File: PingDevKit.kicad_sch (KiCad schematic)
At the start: 47 parts, among them J101 POWER, J102 DEBUG, J103 PORT1, J104 FPGA, J105 ETHERNET, J106 SYNC, J107 SONAR+, J108 SONAR+, J109 SONAR-, J110 SONAR-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

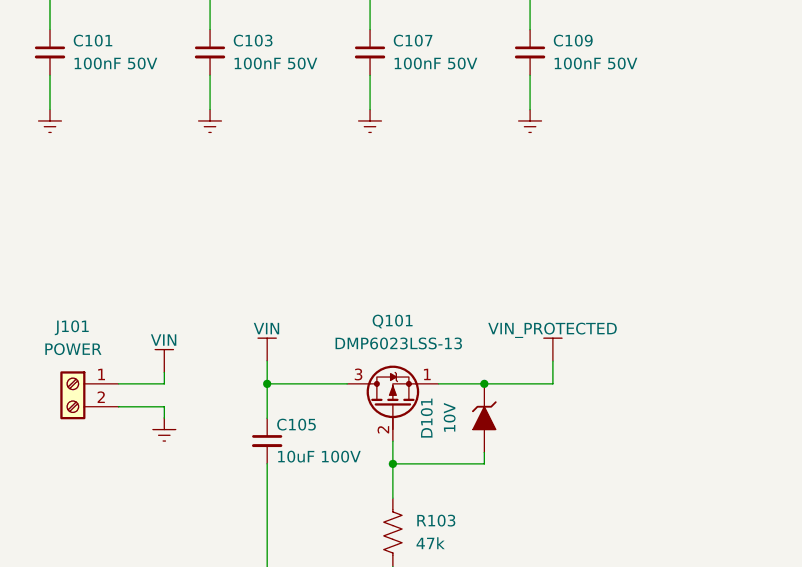
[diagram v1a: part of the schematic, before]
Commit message: ethernet MDI routing
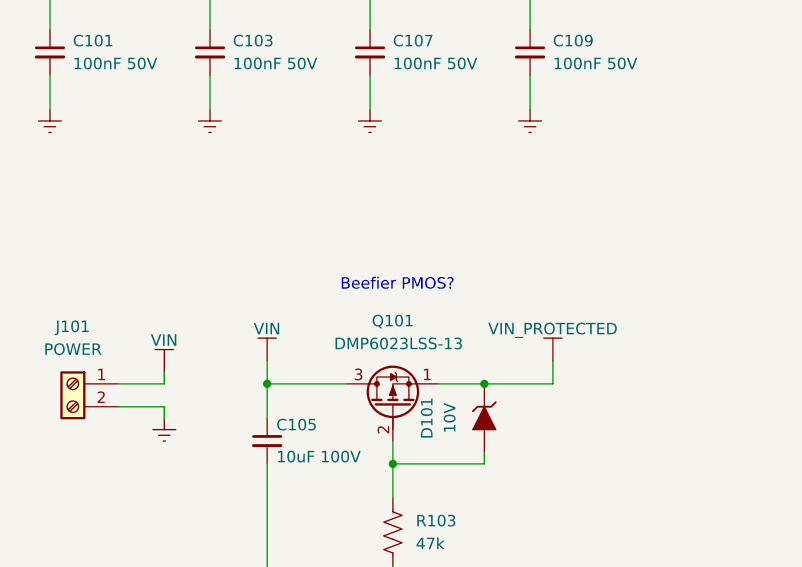
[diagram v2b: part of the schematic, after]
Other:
- note added: "Beefier PMOS?"
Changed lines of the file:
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@@
 		)
 	)
+	(text "Beefier PMOS?"
+		(exclude_from_sim no)
+		(at 69.088 57.658 0)
+		(effects
+			(font
+				(size 1.27 1.27)
+			)
+		)
+	)
 	(text "Gain is from 0 to 60dB from 0.1 to 0.85V "
 		(exclude_from_sim no)
@@
 			(justify right bottom)
 		)
+		(property "Netclass" "MDI"
+			(at 84.074 241.554 0)
+			(effects
+				(font
+					(size 1.27 1.27)
+					(italic yes)
+				)
+				(justify right)
+				(hide yes)
+			)
+		)
 	)
 	(label "ETH{100BASE-T}"
@@
 			(justify right bottom)
 		)
+		(property "Netclass" "MDI"
+			(at 84.074 251.714 0)
+			(effects
+				(font
+					(size 1.27 1.27)
+					(italic yes)
+				)
+				(justify right)
+				(hide yes)
+			)
+		)
 	)
 	(label "SWCLK"
@@
 			(justify right bottom)
 		)
+		(property "Netclass" "MDI"
+			(at 84.074 254.254 0)
+			(effects
+				(font
+					(size 1.27 1.27)
+					(italic yes)
+				)
+				(justify right)
+				(hide yes)
+			)
+		)
 	)
 	(label "OCTOSPI1{OCTOSPI}"
@@
 			(justify right bottom)
 		)
+		(property "Netclass" "MDI"
+			(at 84.074 249.174 0)
+			(effects
+				(font
+					(size 1.27 1.27)
+					(italic yes)
+				)
+				(justify right)
+				(hide yes)
+			)
+		)
 	)

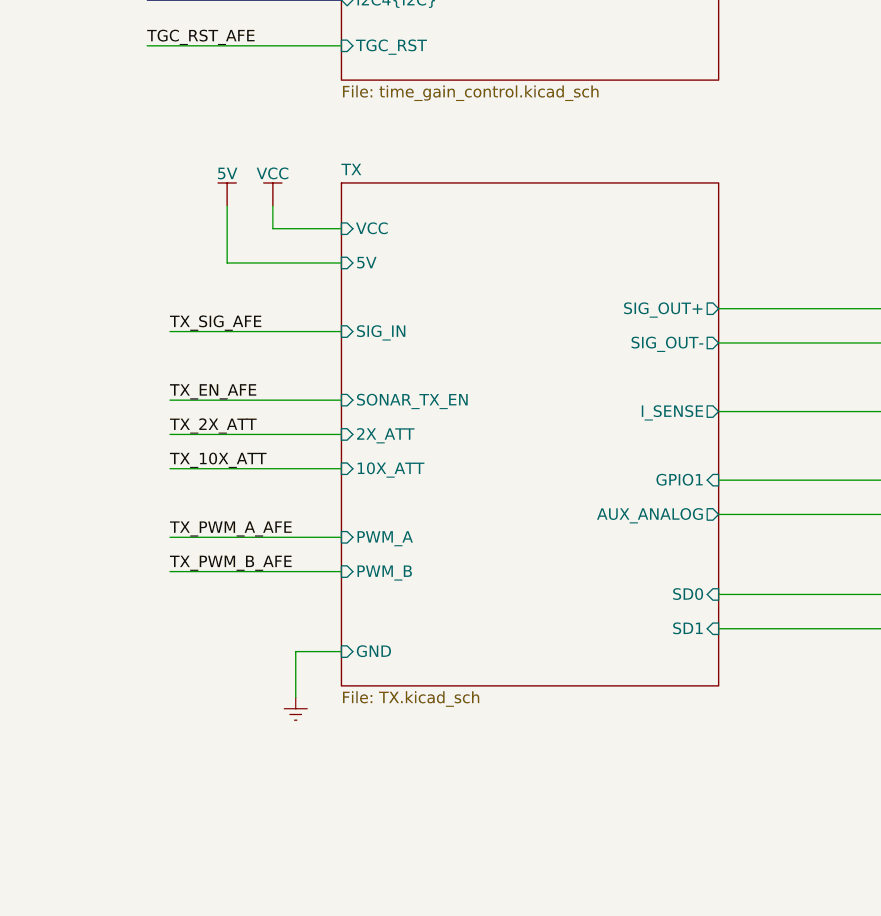
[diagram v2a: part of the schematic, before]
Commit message: bigger board outline + initial integration placements
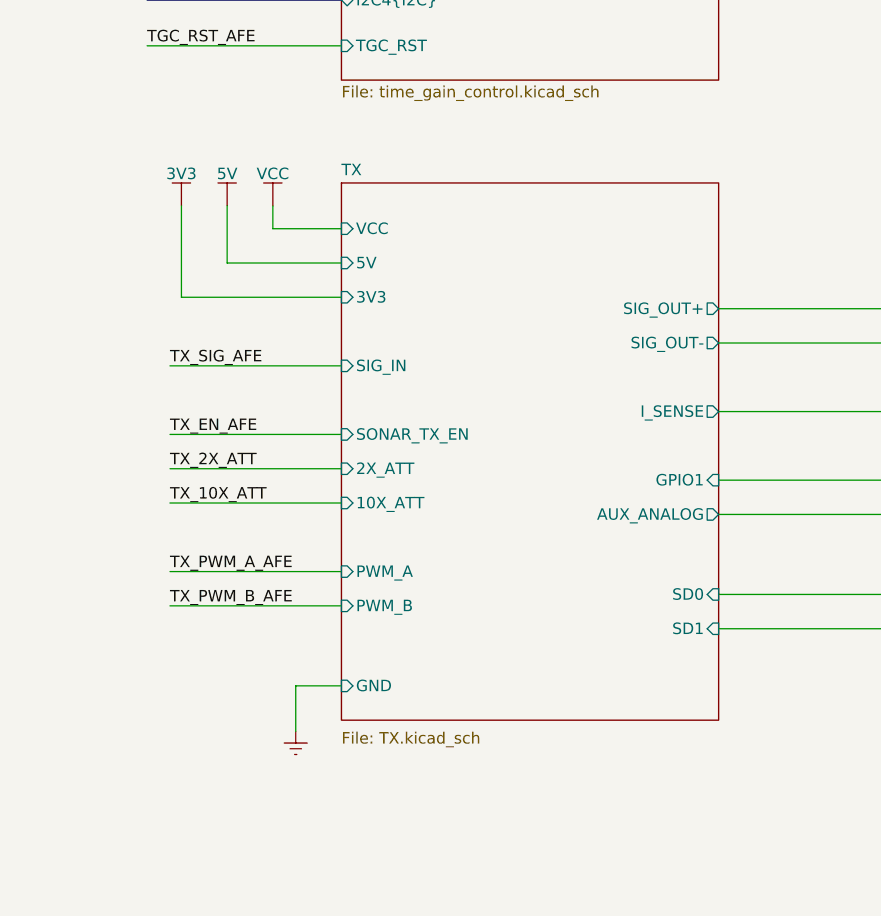
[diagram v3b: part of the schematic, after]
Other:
- sheet TX ports: added 3V3; removed none
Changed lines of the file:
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@@
 	(wire
 		(pts
-			(xy 180.34 246.38) (xy 180.34 251.46)
+			(xy 180.34 250.19) (xy 180.34 255.27)
 		)
 		(stroke
@@
 	(wire
 		(pts
-			(xy 166.37 210.82) (xy 185.42 210.82)
+			(xy 166.37 214.63) (xy 185.42 214.63)
 		)
 		(stroke
@@
 	(wire
 		(pts
-			(xy 166.37 222.25) (xy 185.42 222.25)
+			(xy 166.37 226.06) (xy 185.42 226.06)
 		)
 		(stroke
@@
 	(wire
 		(pts
+			(xy 167.64 196.85) (xy 167.64 207.01)
+		)
+		(stroke
+			(width 0)
+			(type default)
+		)
+	)
+	(wire
+		(pts
 			(xy 55.88 105.41) (xy 55.88 106.68)
 		)
@@
 	(wire
 		(pts
-			(xy 166.37 218.44) (xy 185.42 218.44)
+			(xy 166.37 222.25) (xy 185.42 222.25)
 		)
 		(stroke
@@
 	(wire
 		(pts
-			(xy 180.34 246.38) (xy 185.42 246.38)
+			(xy 180.34 250.19) (xy 185.42 250.19)
 		)
 		(stroke
@@
 	(wire
 		(pts
+			(xy 167.64 207.01) (xy 185.42 207.01)
+		)
+		(stroke
+			(width 0)
+			(type default)
+		)
+	)
+	(wire
+		(pts
 			(xy 227.33 54.61) (xy 238.76 54.61)
 		)
@@
 	(wire
 		(pts
-			(xy 166.37 233.68) (xy 185.42 233.68)
+			(xy 166.37 237.49) (xy 185.42 237.49)
 		)
 		(stroke
@@
 	(wire
 		(pts
-			(xy 166.37 237.49) (xy 185.42 237.49)
+			(xy 166.37 241.3) (xy 185.42 241.3)
 		)
 		(stroke
@@
 	(wire
 		(pts
-			(xy 166.37 226.06) (xy 185.42 226.06)
+			(xy 166.37 229.87) (xy 185.42 229.87)
 		)
 		(stroke
@@
 	)
 	(label "TX_2X_ATT"
-		(at 166.37 222.25 0)
+		(at 166.37 226.06 0)
 		(effects
 			(font
@@
 	)
 	(label "TX_10X_ATT"
-		(at 166.37 226.06 0)
+		(at 166.37 229.87 0)
 		(effects
 			(font
@@
 	)
 	(label "TX_SIG_AFE"
-		(at 166.37 210.82 0)
+		(at 166.37 214.63 0)
 		(effects
 			(font
@@
 	)
 	(label "TX_PWM_B_AFE"
-		(at 166.37 237.49 0)
+		(at 166.37 241.3 0)
 		(effects
 			(font
@@
 	)
 	(label "TX_EN_AFE"
-		(at 166.37 218.44 0)
+		(at 166.37 222.25 0)
 		(effects
 			(font
@@
 	)
 	(label "TX_PWM_A_AFE"
-		(at 166.37 233.68 0)
+		(at 166.37 237.49 0)
 		(effects
 			(font
@@
 	(symbol
 		(lib_id "BR_Virtual_Parts:GND")
-		(at 180.34 251.46 0)
+		(at 180.34 255.27 0)
 		(unit 1)
 		(exclude_from_sim no)
@@
 		(fields_autoplaced yes)
 		(property "Reference" "#PWR0134"
-			(at 180.34 257.81 0)
+			(at 180.34 261.62 0)
 			(effects
 				(font
@@
 		)
 		(property "Value" "GND"
-			(at 180.34 256.54 0)
+			(at 180.34 260.35 0)
 			(effects
 				(font
@@
 		)
 		(property "Footprint" ""
-			(at 180.34 251.46 0)
+			(at 180.34 255.27 0)
 			(effects
 				(font
@@
 		)
 		(property "Datasheet" ""
-			(at 180.34 251.46 0)
+			(at 180.34 255.27 0)
 			(effects
 				(font
@@
 		)
 		(property "Description" ""
-			(at 180.34 251.46 0)
+			(at 180.34 255.27 0)
 			(effects
 				(font
@@
 	(symbol
 		(lib_id "BR_Virtual_Parts:VCC")
+		(at 167.64 196.85 0)
+		(unit 1)
+		(exclude_from_sim no)
+		(in_bom yes)
+		(on_board yes)
+		(dnp no)
+		(property "Reference" "#PWR0154"
+			(at 167.64 200.66 0)
+			(effects
+				(font
+					(size 1.27 1.27)
+				)
+				(hide yes)
+			)
+		)
+		(property "Value" "3V3"
+			(at 167.64 193.294 0)
+			(effects
+				(font
+					(size 1.27 1.27)
+				)
+			)
+		)
+		(property "Footprint" ""
+			(at 167.64 196.85 0)
+			(effects
+				(font
+					(size 1.27 1.27)
+				)
+				(hide yes)
+			)
+		)
+		(property "Datasheet" ""
+			(at 167.64 196.85 0)
+			(effects
+				(font
+					(size 1.27 1.27)
+				)
+				(hide yes)
+			)
+		)
+		(property "Description" "Power symbol creates a global label with name \"VCC\""
+			(at 167.64 196.85 0)
+			(effects
+				(font
+					(size 1.27 1.27)
+				)
+				(hide yes)
+			)
+		)
+		(pin "1"
+		)
+		(instances
+			(project "PingDevKit"
+				(path "/2a5ce3ef-537a-4122-a1be-ef76186bc0d7"
+					(reference "#PWR0154")
+					(unit 1)
+				)
+			)
+		)
+	)
+	(symbol
+		(lib_id "BR_Virtual_Parts:VCC")
 		(at 384.81 45.72 0)
 		(unit 1)
@@
 	(sheet
 		(at 185.42 194.31)
-		(size 41.91 55.88)
+		(size 41.91 59.69)
 		(exclude_from_sim no)
 		(in_bom yes)
 		(on_board yes)
 		(dnp no)
-		(fields_autoplaced yes)
 		(stroke
 			(width 0.1524)
@@
 		)
 		(property "Sheetfile" "TX.kicad_sch"
-			(at 185.42 250.7746 0)
+			(at 185.42 255.27 0)
 			(effects
 				(font
@@
 		)
 		(pin "GND" input
-			(at 185.42 246.38 180)
+			(at 185.42 250.19 180)
 			(effects
 				(font
@@
 		)
 		(pin "SIG_IN" input
-			(at 185.42 210.82 180)
+			(at 185.42 214.63 180)
 			(effects
 				(font
@@
 		)
 		(pin "SONAR_TX_EN" input
-			(at 185.42 218.44 180)
+			(at 185.42 222.25 180)
 			(effects
 				(font
@@
 		)
 		(pin "2X_ATT" input
-			(at 185.42 222.25 180)
+			(at 185.42 226.06 180)
 			(effects
 				(font
@@
 		)
 		(pin "10X_ATT" input
-			(at 185.42 226.06 180)
+			(at 185.42 229.87 180)
 			(effects
 				(font
@@
 		)
 		(pin "PWM_A" input
-			(at 185.42 233.68 180)
+			(at 185.42 237.49 180)
 			(effects
 				(font
@@
 		)
 		(pin "PWM_B" input
-			(at 185.42 237.49 180)
+			(at 185.42 241.3 180)
 			(effects
 				(font
@@
 			)
 		)
+		(pin "3V3" input
+			(at 185.42 207.01 180)
+			(effects
+				(font
+					(size 1.27 1.27)
+				)
+				(justify left)
+			)
+		)

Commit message: adding test pads + minor schematic edits
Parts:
- added GL101: ~, BR_Virtual_Parts:BR_Logo, symbol BR_Virtual_Parts:BR_Logo
- added GL102: ~, BR_Virtual_Parts:JLC_Number, symbol BR_Virtual_Parts:JLC_Number
- added PCB101: Unpopulated PCB, BR_Virtual_Parts:BR_NUMS, symbol BR_Virtual_Parts:PCB
- added TP101: VIN_PROTECTED, BR_Connectors:TEST-TH_BD2.54-P1.4_RED, symbol BR_Connectors:TP_Ring_PTH
- added TP102: GND, BR_Connectors:TEST-TH_BD2.54-P1.4_RED, symbol BR_Connectors:TP_Ring_PTH
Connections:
- net GND: now also TP102.1
- net VIN_PROTECTED: now also TP101.1

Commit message: more test points+ routing improvements
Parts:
- removed GL101: ~, BR_Virtual_Parts:BR_Logo, symbol BR_Virtual_Parts:BR_Logo
- added GL101: ~, BR_Virtual_Parts:BR_Logo_BIG, symbol BR_Virtual_Parts:BR_Logo_BIG
- added TP103: SONAR+, BR_Connectors:TEST-TH_BD2.54-P1.4_RED, symbol BR_Connectors:TP_Ring_PTH
- added TP104: SONAR-, BR_Connectors:TEST-TH_BD2.54-P1.4_RED, symbol BR_Connectors:TP_Ring_PTH
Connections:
- net SONAR+: now also TP103.1
- net SONAR-: now also TP104.1

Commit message: some moving around
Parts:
- J111: footprint BR_Connectors_JST:SM02B-GHS-TB -> BR_Connector_JST_misc:SM02B-PASS-TBT; symbol BR_Connectors_JST_GH:SM02B-GHS-TB -> BR_Connectors_JST_PA:SM02B-PASS-TBT; BRE Number BRE-000100 -> BRE-000105; JLCPCB Part Num C189893 -> C265417; Manufacturer Part Num SM02B-GHS-TB -> SM02B-PASS-TBT; Supplier 2 DigiKey -> Mouser; Supplier Part Num 1 455-1564-1-ND -> 455-SM02B-PASS-TBTCT-ND; Supplier Part Num 2 455-1564-2-ND -> 306-SM02BPASSTBTLFSN; Supplier Part Num 3 C189893 -> C265417
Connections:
- net GND: now also J111.MP1, J111.MP2; no longer J111.MP
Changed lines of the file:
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@@
 		(color 0 0 0 0)
 	)
+	(junction
+		(at 247.65 367.03)
+		(diameter 0)
+		(color 0 0 0 0)
+	)
 	(no_connect
 		(at 77.47 237.49)
@@
 	(wire
 		(pts
-			(xy 215.9 359.41) (xy 242.57 359.41)
+			(xy 215.9 359.41) (xy 243.84 359.41)
 		)
 		(stroke
@@
 	(wire
 		(pts
+			(xy 250.19 367.03) (xy 247.65 367.03)
+		)
+		(stroke
+			(width 0)
+			(type default)
+		)
+	)
+	(wire
+		(pts
 			(xy 166.37 214.63) (xy 185.42 214.63)
 		)
@@
 		)
 	)
+	(wire
+		(pts
+			(xy 247.65 365.76) (xy 247.65 367.03)
+		)
+		(stroke
+			(width 0)
+			(type default)
+		)
+	)
 	(bus
 		(pts
@@
 	(wire
 		(pts
-			(xy 227.33 361.95) (xy 242.57 361.95)
+			(xy 227.33 361.95) (xy 243.84 361.95)
 		)
 		(stroke
@@
 	(wire
 		(pts
+			(xy 247.65 367.03) (xy 247.65 368.3)
+		)
+		(stroke
+			(width 0)
+			(type default)
+		)
+	)
+	(wire
+		(pts
 			(xy 227.33 97.79) (xy 290.83 97.79)
 		)
@@
 	(wire
 		(pts
+			(xy 247.65 355.6) (xy 247.65 354.33)
+		)
+		(stroke
+			(width 0)
+			(type default)
+		)
+	)
+	(wire
+		(pts
 			(xy 180.34 250.19) (xy 185.42 250.19)
 		)
@@
 	(wire
 		(pts
+			(xy 247.65 354.33) (xy 250.19 354.33)
+		)
+		(stroke
+			(width 0)
+			(type default)
+		)
+	)
+	(wire
+		(pts
 			(xy 205.74 308.61) (xy 218.44 308.61)
 		)
@@
 	(wire
 		(pts
+			(xy 250.19 354.33) (xy 250.19 367.03)
+		)
+		(stroke
+			(width 0)
+			(type default)
+		)
+	)
+	(wire
+		(pts
 			(xy 43.18 237.49) (xy 30.48 237.49)
 		)
@@
 	)
 	(symbol
-		(lib_id "BR_Connectors_JST_GH:SM02B-GHS-TB")
+		(lib_id "BR_Connectors_JST_PA:SM02B-PASS-TBT")
 		(at 248.92 358.14 0)
 		(mirror y)
@@
 		(on_board yes)
 		(dnp no)
-		(fields_autoplaced yes)
 		(property "Reference" "J111"
-			(at 250.19 359.4099 0)
+			(at 250.952 359.41 0)
 			(effects
 				(font
@@
 		)
 		(property "Value" "TRANSDUCER"
-			(at 250.19 361.9499 0)
+			(at 250.952 361.95 0)
 			(effects
 				(font
@@
 			)
 		)
-		(property "Footprint" "BR_Connectors_JST:SM02B-GHS-TB"
+		(property "Footprint" "BR_Connector_JST_misc:SM02B-PASS-TBT"
 			(at 248.92 281.94 0)
 			(effects
@@
 			)
 		)
-		(property "Datasheet" "https://www.jst-mfg.com/product/pdf/eng/eGH.pdf"
+		(property "Datasheet" "https://www.jst-mfg.com/product/pdf/eng/ePA-F.pdf"
 			(at 248.92 284.48 0)
 			(effects
@@
 			)
 		)
-		(property "Description" "JST-GH Connector 2-pos, P=1.25mm, 1A 50V 30mΩ, 26-30awg, Horizontal"
+		(property "Description" "JST-PA Connector 2-pos, P=2mm, 3A 250V 10mΩ, 22-28awg, Horizontal"
 			(at 248.92 287.02 0)
 			(effects
@@
 			)
 		)
-		(property "Manufacturer Part Num" "SM02B-GHS-TB"
+		(property "Manufacturer Part Num" "SM02B-PASS-TBT"
 			(at 248.92 292.1 0)
 			(effects
@@
 			)
 		)
-		(property "BRE Number" "BRE-000100"
+		(property "BRE Number" "BRE-000105"
 			(at 248.92 294.64 0)
 			(effects
@@
 			)
 		)
-		(property "Supplier Part Num 1" "455-1564-1-ND"
+		(property "Supplier Part Num 1" "455-SM02B-PASS-TBTCT-ND"
 			(at 248.92 299.72 0)
 			(effects
@@
 		)
 		(property "Supplier 3" "JLCPCB"
-			(at 248.92 302.26 0)
+			(at 248.92 307.34 0)
 			(effects
 				(font
@@
 			)
 		)
-		(property "Supplier Part Num 3" "C189893"
-			(at 248.92 304.8 0)
+		(property "Supplier Part Num 3" "C265417"
+			(at 248.92 309.88 0)
 			(effects
 				(font
@@
 			)
 		)
-		(property "Supplier 2" "DigiKey"
-			(at 248.92 307.34 0)
+		(property "Supplier 2" "Mouser"
+			(at 248.92 302.26 0)
 			(effects
 				(font
@@
 			)
 		)
-		(property "Supplier Part Num 2" "455-1564-2-ND"
-			(at 248.92 309.88 0)
+		(property "Supplier Part Num 2" "306-SM02BPASSTBTLFSN"
+			(at 248.92 304.8 0)
 			(effects
 				(font
@@
 			)
 		)
-		(property "JLCPCB Part Num" "C189893"
-			(at 248.92 317.5 0)
+		(property "JLCPCB Part Num" "C265417"
+			(at 248.92 312.42 0)
 			(effects
 				(font
@@
 		(pin "1"
 		)
-		(pin "MP"
+		(pin "MP2"
 		)
 		(pin "2"
 		)
+		(pin "MP1"
+		)
 		(instances
 			(project "SonarDevBoard"
@@
 	(symbol
 		(lib_id "BR_Virtual_Parts:GND")
-		(at 247.65 367.03 0)
+		(at 247.65 368.3 0)
 		(mirror y)
 		(unit 1)
@@
 		(fields_autoplaced yes)
 		(property "Reference" "#PWR0141"
-			(at 247.65 373.38 0)
+			(at 247.65 374.65 0)
 			(effects
 				(font
@@
 		)
 		(property "Value" "GND"
-			(at 247.65 372.11 0)
+			(at 247.65 373.38 0)
 			(effects
 				(font
@@
 		)
 		(property "Footprint" ""
-			(at 247.65 367.03 0)
+			(at 247.65 368.3 0)
 			(effects
 				(font
@@
 		)
 		(property "Datasheet" ""
-			(at 247.65 367.03 0)
+			(at 247.65 368.3 0)
 			(effects
 				(font
@@
 		)
 		(property "Description" ""
-			(at 247.65 367.03 0)
+			(at 247.65 368.3 0)
 			(effects
 				(font
